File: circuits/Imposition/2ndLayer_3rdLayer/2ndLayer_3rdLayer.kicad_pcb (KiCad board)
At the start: 2 copper layers, 123.9 x 37.4 mm, 182 parts, among them J1 Conn_01x10_Pin, J10 Conn_01x06_MountingPin, J11 Conn_01x06_MountingPin, J2 Conn_02x10_Odd_Even, J3 Conn_02x10_Odd_Even, J4 USB_C_Receptacle_USB2.0, Q1 SSM3J332R, Q10 S8550, Q11 SSM3J332R, Q12 S8550, Q13 S8550, Q14 S8550, Q15 2N7002, Q16 2N7002, Q17 SSM3J332R, Q18 2N7002, Q2 S8550, Q3 SSM3J332R, Q4 S8550, Q7 SSM6J808R, Q8 2N7002, Q9 SSM6J808R, SW1 SW_SPST, SW10 SW_DIP_x04, SW2 SW_SPDT_White, SW3 SW_SPST, SW4 SW_SPST, SW5 SW_DIP_x04, SW6 SW_SPDT, SW7 SW_SPST, SW8 SW_SPST, SW9 SW_SPST, U1 DCDC_TPSM336x5, U10 FT231XS, U2 TWE-L-WX, U3 MAX3485, U4 MAX3485, U5 MAX3485, U6 MAX3485, U7 AZ1117CH-3.3, U8 STM32H723VGTx, U9 Display_Akzk_128x68OLED, Y1 16MHz

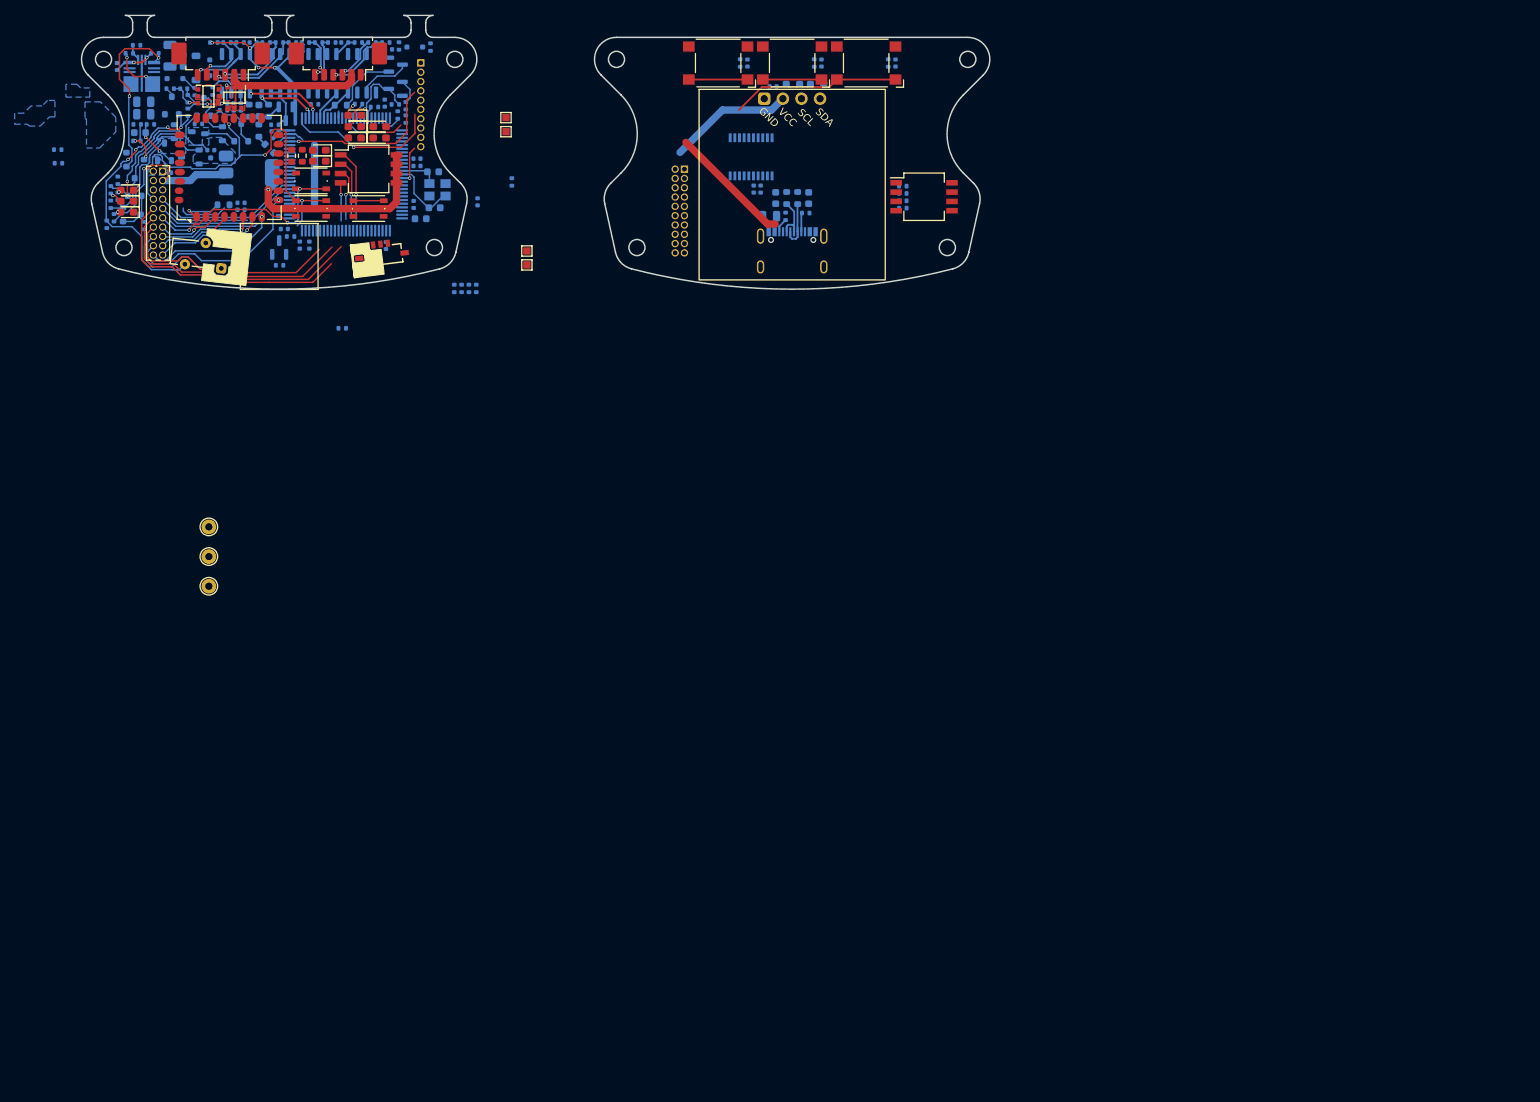
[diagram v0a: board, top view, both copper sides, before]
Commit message: 発注_第一弾
Drive, 1stLayer_Power, 2ndLayer_3rdLayer
を発注
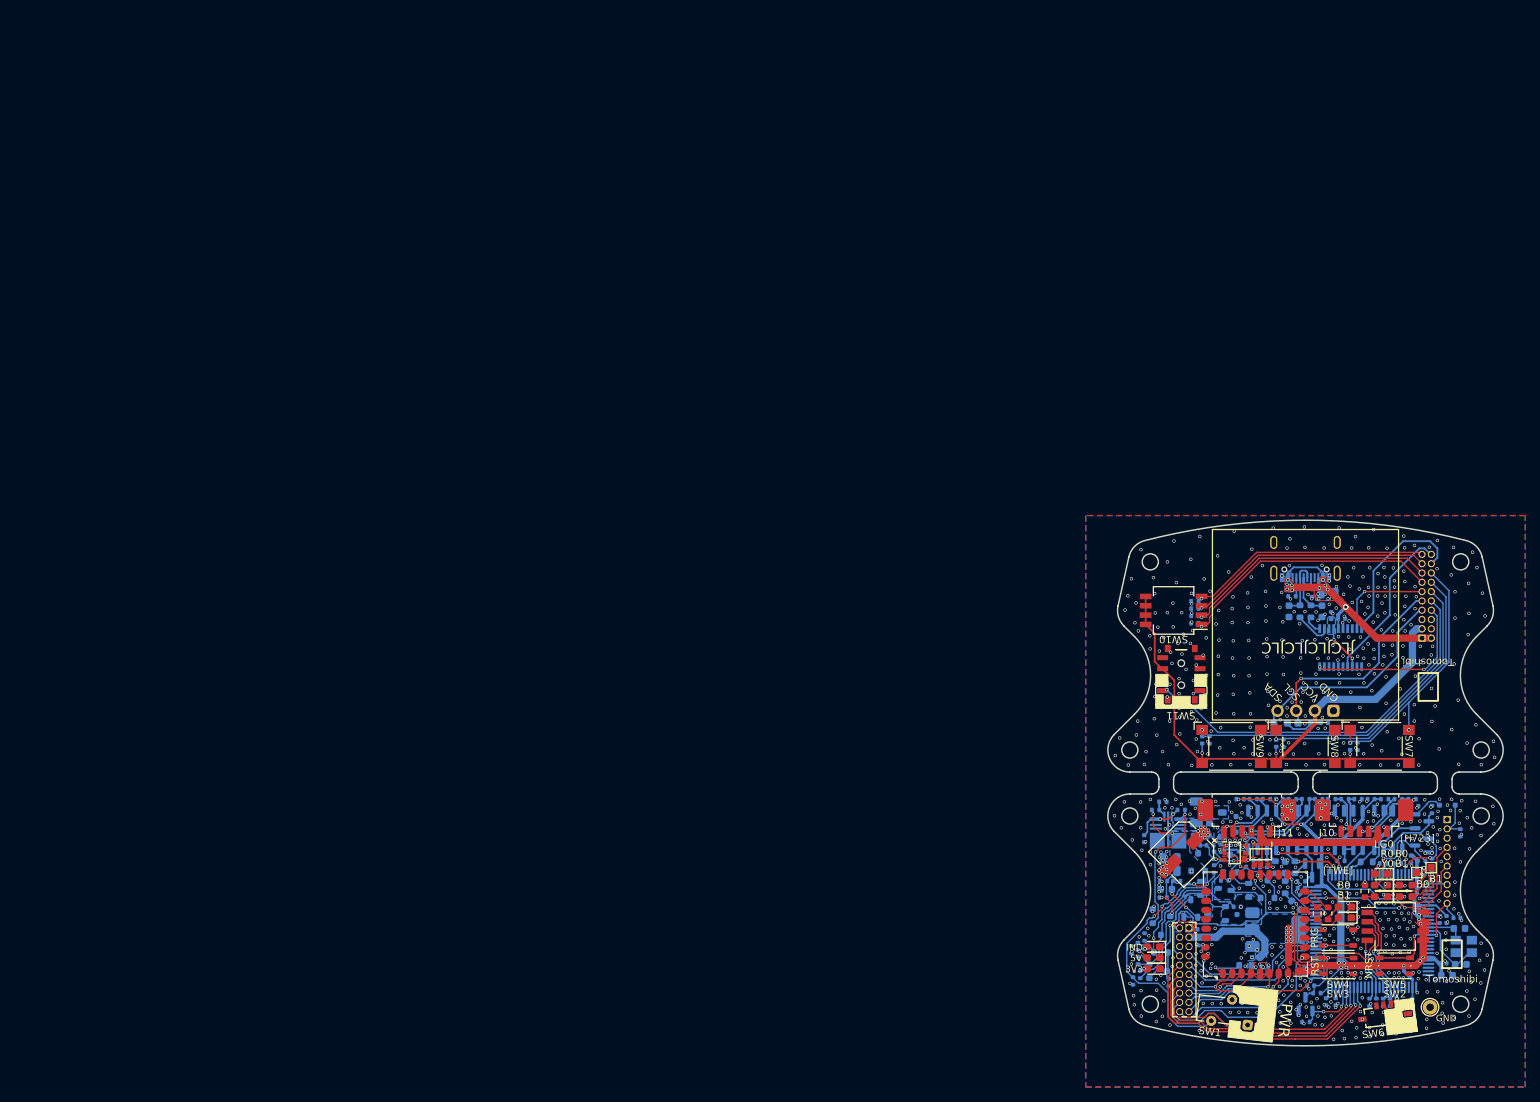
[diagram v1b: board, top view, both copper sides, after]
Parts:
- removed H3, H4: MountingHole_Pad, TestPoint:TestPoint_Pad_1.0x1.0mm
- removed TP2, TP3: TestPoint, TestPoint:TestPoint_THTPad_D2.0mm_Drill1.0mm
- added C21: 47uF, Capacitor_SMD:CP_Elec_6.3x5.4, F.Cu at (123.5, 111.2)
- added R80: 10k, Resistor_SMD:R_0402_1005Metric, B.Cu at (121.1, 88.5)
- added SW11: SW_SPDT, TomoshibiLibrary:SW_Slide_DPDT_SSSS820101, F.Cu at (123.1, 86.9)
- R37, R38: value 10k -> PullUP?
- R66: footprint Resistor_SMD:R_0402_1005Metric -> Resistor_SMD:R_0603_1608Metric; moved to F.Cu
- moved R29 188.4 mm to (125.5, 123.4), turned to 90 degrees
- moved R17 182.7 mm to (116.3, 124.5), turned to 90 degrees
- moved TP1 179.1 mm to (157.1, 132.3)
- moved R1 176.8 mm to (161.2, 108.5)
- moved C33 175.4 mm to (118.0, 109.3), turned to -90 degrees
- moved R5 175.3 mm to (157.3, 105.4)
- moved R39 175.2 mm to (143.1, 119.5)
- moved D1 174.8 mm to (159.4, 104.8)
- moved C3 174.7 mm to (159.3, 120.4), turned to -90 degrees
- moved C27 174.5 mm to (158.8, 126.3), turned to 0 degrees
- moved SW3 174.2 mm to (144.6, 126.7)
- moved D13 174.2 mm to (153.8, 117.2)
- moved D15 174.2 mm to (150.3, 117.2)
- moved D16 174.1 mm to (150.4, 115.7)
- moved D12 174.1 mm to (153.8, 115.7)
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- renumbered SW2 to SW1, SW1 to SW2
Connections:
- C12 pad 1: +3.3V -> /3rdLayer/3V3_3rdLayer
- C14 pad 1: +3.3V -> /3rdLayer/3V3_3rdLayer
- C34 pad 1: +3.3V -> /3rdLayer/3V3_3rdLayer
- C35 pad 1: +3.3V -> /3rdLayer/3V3_3rdLayer
- C36 pad 1: VBUS -> /3rdLayer/VBUS_3rdLayer
- C37 pad 2: VBUS -> /3rdLayer/VBUS_3rdLayer
- J1 pad 1: unconnected-(J1-Pin_1-Pad1) -> GND
- J1 pad 10: unconnected-(J1-Pin_10-Pad10) -> /2ndLayer/NRST
- J1 pad 2: unconnected-(J1-Pin_2-Pad2) -> Net-(D1-K)
- J1 pad 3: unconnected-(J1-Pin_3-Pad3) -> GND
- J1 pad 4: unconnected-(J1-Pin_4-Pad4) -> /2ndLayer/SWDIO
- J1 pad 5: unconnected-(J1-Pin_5-Pad5) -> GND
- J1 pad 6: unconnected-(J1-Pin_6-Pad6) -> /2ndLayer/SWCLK
- J1 pad 7: unconnected-(J1-Pin_7-Pad7) -> GND
- J1 pad 8: unconnected-(J1-Pin_8-Pad8) -> /2ndLayer/SWO
- J1 pad 9: unconnected-(J1-Pin_9-Pad9) -> GND
- J2 pad 10: unconnected-(J2-Pin_10-Pad10) -> /2ndLayer/SlideSW1
- J2 pad 12: unconnected-(J2-Pin_12-Pad12) -> /2ndLayer/TactSW2
- J2 pad 14: unconnected-(J2-Pin_14-Pad14) -> /2ndLayer/TactSW1
- J2 pad 16: unconnected-(J2-Pin_16-Pad16) -> /2ndLayer/TactSW0
- J3 pad 1: VBUS -> /3rdLayer/VBUS_3rdLayer
- J3 pad 10: unconnected-(J3-Pin_10-Pad10) -> /3rdLayer/SlideSW1
- J3 pad 11: /3rdLayer/DIPSW1 -> /3rdLayer/PRG_Twe
- J3 pad 12: unconnected-(J3-Pin_12-Pad12) -> /3rdLayer/TactSW2
- J3 pad 13: /3rdLayer/DIPSW2 -> /3rdLayer/DIPSW0
- J3 pad 14: unconnected-(J3-Pin_14-Pad14) -> /3rdLayer/TactSW1
- J3 pad 15: /3rdLayer/DIPSW3 -> /3rdLayer/DIPSW1
- J3 pad 16: unconnected-(J3-Pin_16-Pad16) -> /3rdLayer/TactSW0
- J3 pad 17: /3rdLayer/PRG_Twe -> /3rdLayer/DIPSW2
- J3 pad 18: unconnected-(J3-Pin_18-Pad18) -> /3rdLayer/TweWriteTX_TweRX
- J3 pad 19: /3rdLayer/RST_Twe -> /3rdLayer/DIPSW3
- J3 pad 2: VBUS -> /3rdLayer/VBUS_3rdLayer
- J3 pad 20: unconnected-(J3-Pin_20-Pad20) -> /3rdLayer/TweWriteRX_TweTX
- J3 pad 3: GND -> /3rdLayer/3V3_3rdLayer
- J3 pad 4: +3.3V -> GND
- J3 pad 7: GND -> /3rdLayer/I2C_SDA
- J3 pad 8: unconnected-(J3-Pin_8-Pad8) -> /3rdLayer/RST_Twe
- J3 pad 9: /3rdLayer/DIPSW0 -> /3rdLayer/I2C_SCL
- J4 pad A4: VBUS -> /3rdLayer/VBUS_3rdLayer
- J4 pad A9: VBUS -> /3rdLayer/VBUS_3rdLayer
- J4 pad B4: VBUS -> /3rdLayer/VBUS_3rdLayer
- J4 pad B9: VBUS -> /3rdLayer/VBUS_3rdLayer
- R39 pad 2: /2ndLayer/TweLite/LED0 -> /2ndLayer/TweLite/LED_B0
- R40 pad 2: /2ndLayer/TweLite/LED1 -> /2ndLayer/TweLite/LED_B1
- R74 pad 1: +3.3V -> /3rdLayer/3V3_3rdLayer
- R75 pad 1: +3.3V -> /3rdLayer/3V3_3rdLayer
- SW10 pad 5: +3.3V -> /3rdLayer/3V3_3rdLayer
- SW10 pad 6: +3.3V -> /3rdLayer/3V3_3rdLayer
- SW10 pad 7: +3.3V -> /3rdLayer/3V3_3rdLayer
- SW10 pad 8: +3.3V -> /3rdLayer/3V3_3rdLayer
- SW6 pad 1: /2ndLayer/SlideSW0 -> unconnected-(SW6-A-Pad1)
- SW6 pad 3: unconnected-(SW6-C-Pad3) -> /2ndLayer/SlideSW0
- SW7 pad 2: +3.3V -> /3rdLayer/3V3_3rdLayer
- SW8 pad 2: +3.3V -> /3rdLayer/3V3_3rdLayer
- SW9 pad 2: +3.3V -> /3rdLayer/3V3_3rdLayer
- TP1 pad 1: +5V -> GND
- U10 pad 15: VBUS -> /3rdLayer/VBUS_3rdLayer
- U2 pad 14: /2ndLayer/MainRXx_TweTX1 -> /2ndLayer/MainRX1_TweTX1
- U2 pad 15: unconnected-(U2-DIO13/DI2-Pad15) -> /2ndLayer/TweLite/LED_B1
- U2 pad 16: unconnected-(U2-DIO11/DI3-Pad16) -> /2ndLayer/TweLite/LED_B0
- U2 pad 17: /2ndLayer/MainTXx_TweRX1 -> /2ndLayer/MainTX1_TweRX1
- U8 pad 1: unconnected-(U8-PE2-Pad1) -> /2ndLayer/LED_B0
- U8 pad 32: unconnected-(U8-PC4-Pad32) -> /2ndLayer/SlideSW0
- U8 pad 33: unconnected-(U8-PC5-Pad33) -> /2ndLayer/DIPSW0
- U8 pad 34: unconnected-(U8-PB0-Pad34) -> /2ndLayer/DIPSW1
- U8 pad 35: unconnected-(U8-PB1-Pad35) -> /2ndLayer/V_Meas.
- U8 pad 37: unconnected-(U8-PE7-Pad37) -> /2ndLayer/DIPSW2
- U8 pad 38: unconnected-(U8-PE8-Pad38) -> /2ndLayer/DIPSW3
- U8 pad 4: unconnected-(U8-PE5-Pad4) -> /2ndLayer/LED_B1
- U8 pad 42: unconnected-(U8-PE12-Pad42) -> /2ndLayer/SlideSW1
- U8 pad 43: unconnected-(U8-PE13-Pad43) -> /2ndLayer/TactSW2
- U8 pad 44: unconnected-(U8-PE14-Pad44) -> /2ndLayer/TactSW1
- U8 pad 45: unconnected-(U8-PE15-Pad45) -> /2ndLayer/TactSW0
- U8 pad 46: unconnected-(U8-PB10-Pad46) -> /2ndLayer/Main->RST_Twe
- U8 pad 68: unconnected-(U8-PA9-Pad68) -> /2ndLayer/MainTX1_TweRX1
- U8 pad 69: unconnected-(U8-PA10-Pad69) -> /2ndLayer/MainRX1_TweTX1
- U8 pad 86: unconnected-(U8-PD5-Pad86) -> /2ndLayer/LED_Y0
- U8 pad 91: unconnected-(U8-PB5-Pad91) -> /2ndLayer/LED_LG0
- U8 pad 97: unconnected-(U8-PE0-Pad97) -> /2ndLayer/LED_nR0
- U9 pad 2: +3.3V -> /3rdLayer/3V3_3rdLayer
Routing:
- net /3rdLayer/3V3_3rdLayer: track 0.00 -> 99.1 mm, vias 0 -> 3
- net +3.3V: track 114.3 -> 177.1 mm, vias 6 -> 29
- net /3rdLayer/SlideSW1: track 0.00 -> 52.3 mm, vias 0 -> 1
- net /2ndLayer/SlideSW1: track 0.00 -> 39.7 mm, vias 0 -> 1
- net /2ndLayer/TactSW2: track 0.00 -> 36.8 mm, vias 0 -> 1
- net /3rdLayer/DIPSW0: track 0.00 -> 36.1 mm, vias 0 -> 1
- net unconnected-(J2-Pin_12-Pad12): track 35.9 -> 0.00 mm
- net unconnected-(J2-Pin_10-Pad10): track 35.8 -> 0.00 mm
- net /3rdLayer/DIPSW1: track 0.00 -> 35.0 mm, vias 0 -> 1
- net /2ndLayer/TactSW1: track 0.00 -> 34.3 mm, vias 0 -> 1
- net /3rdLayer/DIPSW2: track 0.00 -> 34.0 mm, vias 0 -> 1
- net /3rdLayer/TactSW1: track 8.00 -> 41.9 mm, vias 0 -> 2
- net /2ndLayer/TactSW0: track 0.00 -> 33.7 mm, vias 0 -> 2
- net /3rdLayer/DIPSW3: track 0.00 -> 33.5 mm, vias 0 -> 1
- net /3rdLayer/VBUS_3rdLayer: track 0.00 -> 33.5 mm, vias 0 -> 14
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- added copper zone on B.Cu, net +3.3V
- added copper zone on F.Cu, net +3.3V
- added copper zone on B.Cu, net /3rdLayer/VBUS_3rdLayer
- added copper zone on F.Cu, net /3rdLayer/VBUS_3rdLayer
- added copper zone on B.Cu, net GND
- added copper zone on F.Cu, net GND
- added copper zone on B.Cu, net Net-(U10-3V3OUT)
- added copper zone on B.Cu, net VDD
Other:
- board size 123.9 x 37.4 mm -> 53.9 x 71.7 mm
- board text added: "3V3"
- board text added: "5V"
- board text added: "B0"
- board text added: "B1"
- board text added: "Designed by @cat_nekonekone"
- board text added: "GND"
- board text added: "IND"
- board text added: "JLCJLCJLCJLC"
- board text added: "LG0"
- board text added: "NRST"
- board text added: "PRG"
- board text added: "PWR"
- board text added: "R0"
- board text added: "RST"
- board text added: "Tomoshibi"
- board text added: "Y0"
- board text added: "[H723]"
- board text added: "[TWE]"
- board text added: "燈"
- board text removed: "Slide0のシルク逆"
